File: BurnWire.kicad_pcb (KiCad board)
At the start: 2 copper layers, 44.6 x 45.3 mm, 14 parts, among them J1 B6B-XH-A_LF__SN_, U1 ADP2303ARDZ

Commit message: done layout
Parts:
- moved R3 26.6 mm to (139.1, 75.4), turned to 0 degrees
- moved U1 26.0 mm to (137.8, 88.3), turned to -90 degrees
- moved R1 25.1 mm to (144.7, 93.8)
- moved C3 24.3 mm to (160.8, 79.2)
- moved C4 24.3 mm to (169.8, 79.2)
- moved C5 24.3 mm to (165.8, 88.6)
- moved TP2 23.0 mm to (149.1, 89.5)
- moved R2 20.9 mm to (143.9, 85.0)
- moved J1 19.0 mm to (142.2, 79.7), turned to 180 degrees
- moved CR1 11.8 mm to (157.2, 98.0), turned to 180 degrees
- moved L1 11.4 mm to (153.7, 79.2)
- moved TP1 10.2 mm to (158.6, 106.5)
- moved C2 9.40 mm to (134.6, 98.8)
- moved C1 6.34 mm to (134.4, 106.4)
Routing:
- net /VBatt: track 105.4 -> 34.9 mm
- net /EN: track 47.2 -> 8.22 mm, vias 2 -> 0
- net Net-(U1-SW): track 34.9 -> 68.0 mm, vias 0 -> 2
- net Net-(U1-PGOOD): track 44.7 -> 13.1 mm, vias 2 -> 0
- net GND: track 159.1 -> 165.0 mm
- net /Vout: track 38.6 -> 42.9 mm
- net /VCutN: track 32.6 -> 29.6 mm, vias 0 -> 2
- net Net-(U1-BST): track 21.6 -> 23.9 mm
- net Net-(U1-FB): track 7.55 -> 5.95 mm
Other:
- board size 44.6 x 45.3 mm -> 44.6 x 45.4 mm

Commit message: optimized layout
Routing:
- net GND: track 165.0 -> 161.6 mm
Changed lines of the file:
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@@
-	)
-	(segment
-		(start 158.1685 71.2185)
-		(end 160.35 73.4)
-		(width 0.635)
-		(layer "F.Cu")
-		(net 3)
 	)
 	(segment
@@
 	)
 	(segment
-		(start 143.3815 71.2185)
-		(end 158.1685 71.2185)
-		(width 0.635)
-		(layer "F.Cu")
-		(net 3)
-	)
-	(segment
-		(start 140.75 73.85)
-		(end 143.3815 71.2185)
-		(width 0.635)
-		(layer "F.Cu")
-		(net 3)
-	)
-	(segment
 		(start 136.8 89.27)
 		(end 137.8 88.27)
@@
 	)
 	(segment
-		(start 160.35 73.4)
+		(start 143.851597 73.4)
 		(end 164.9 73.4)
 		(width 0.635)
@@
 	)
 	(segment
-		(start 140.7635 76.8365)
-		(end 140.7635 73.8635)
+		(start 138.4 79.2)
+		(end 138.4 78.851597)
 		(width 0.635)
 		(layer "F.Cu")
@@
 	)
 	(segment
-		(start 140.7635 73.8635)
-		(end 140.75 73.85)
-		(width 0.635)
-		(layer "F.Cu")
-		(net 3)
-	)
-	(segment
 		(start 164.583431 108.7535)
 		(end 166.5 106.836931)
@@
 	)
 	(segment
+		(start 138.4 78.851597)
+		(end 143.851597 73.4)
+		(width 0.635)
+		(layer "F.Cu")
+		(net 3)
+	)
+	(segment
 		(start 149.55 101.047692)
 		(end 149.55 98.7925)
@@
 		(width 0.635)
 		(layer "F.Cu")
-		(net 3)
-	)
-	(segment
-		(start 138.4 79.2)
-		(end 140.7635 76.8365)
-		(width 0.635)
-		(layer "F.Cu")

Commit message: generated gerber
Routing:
- net GND: track 161.6 -> 167.7 mm
- net /Vout: track 42.9 -> 47.6 mm
- net /VBatt: track 34.9 -> 35.6 mm

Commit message: redid layout
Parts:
- moved L1 32.8 mm to (141.5, 109.7)
- moved C1 28.6 mm to (163.1, 105.9), turned to 180 degrees
- moved C2 28.3 mm to (162.8, 99.0), turned to 180 degrees
- moved U1 18.3 mm to (155.6, 92.7), turned to 180 degrees
- moved CR1 17.4 mm to (169.4, 110.4)
- moved TP2 16.9 mm to (140.6, 104.2)
- moved R2 13.1 mm to (135.2, 94.7)
- moved R3 10.5 mm to (137.9, 85.8)
- moved TP1 7.08 mm to (153.1, 111.0)
- moved C4 4.32 mm to (168.6, 83.3)
- moved C5 4.23 mm to (168.6, 91.8)
- moved R1 3.80 mm to (143.9, 97.5), turned to -90 degrees
- moved C3 3.76 mm to (158.8, 82.4)
- moved J1 1.68 mm to (141.7, 81.3)
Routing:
- net /EN: track 8.22 -> 100.3 mm
- net GND: track 167.7 -> 87.8 mm
- net Net-(U1-SW): track 68.0 -> 27.4 mm, vias 2 -> 0
- net /VBatt: track 35.6 -> 14.4 mm
- net Net-(U1-FB): track 5.95 -> 23.8 mm
- net /VCutN: track 29.4 -> 44.5 mm, vias 2 -> 0
- net /Vout: track 47.6 -> 33.8 mm
- net Net-(U1-BST): track 23.9 -> 13.4 mm
- net Net-(U1-PGOOD): track 13.1 -> 21.7 mm

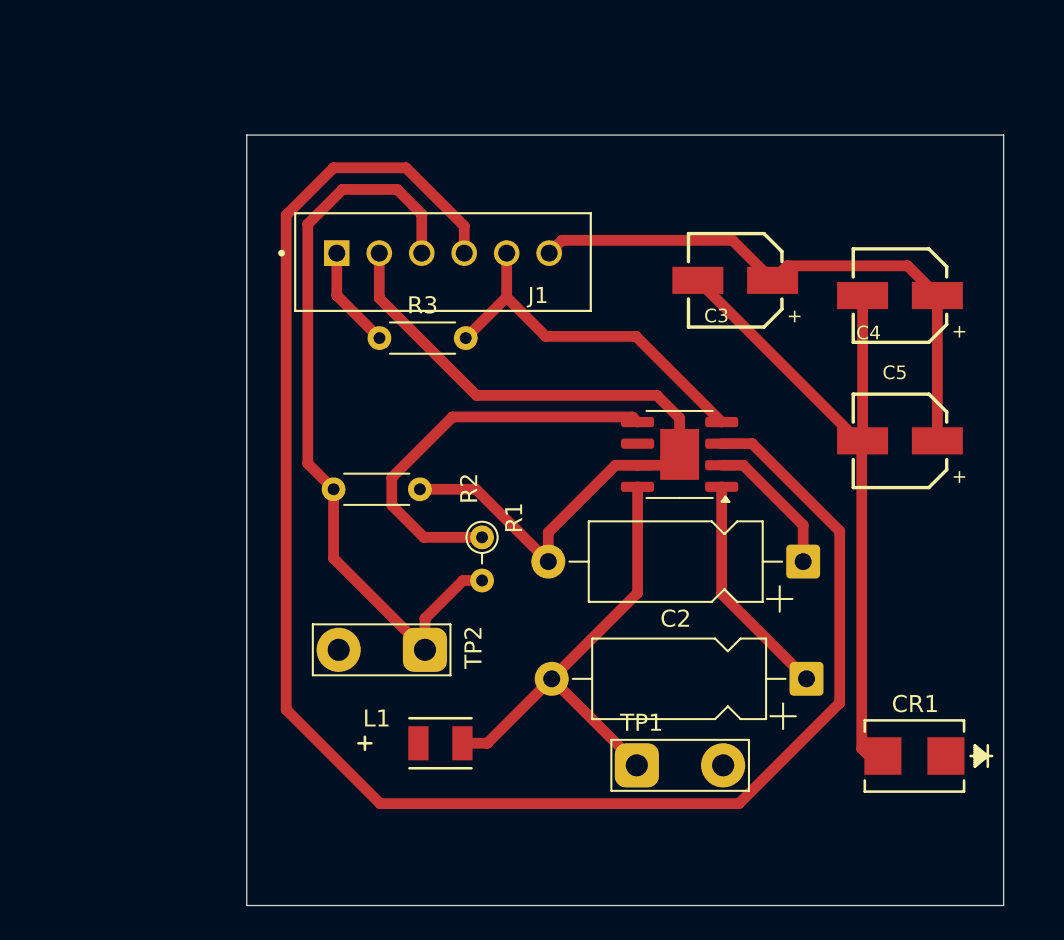
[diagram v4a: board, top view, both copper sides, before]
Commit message: finished one-layer layout
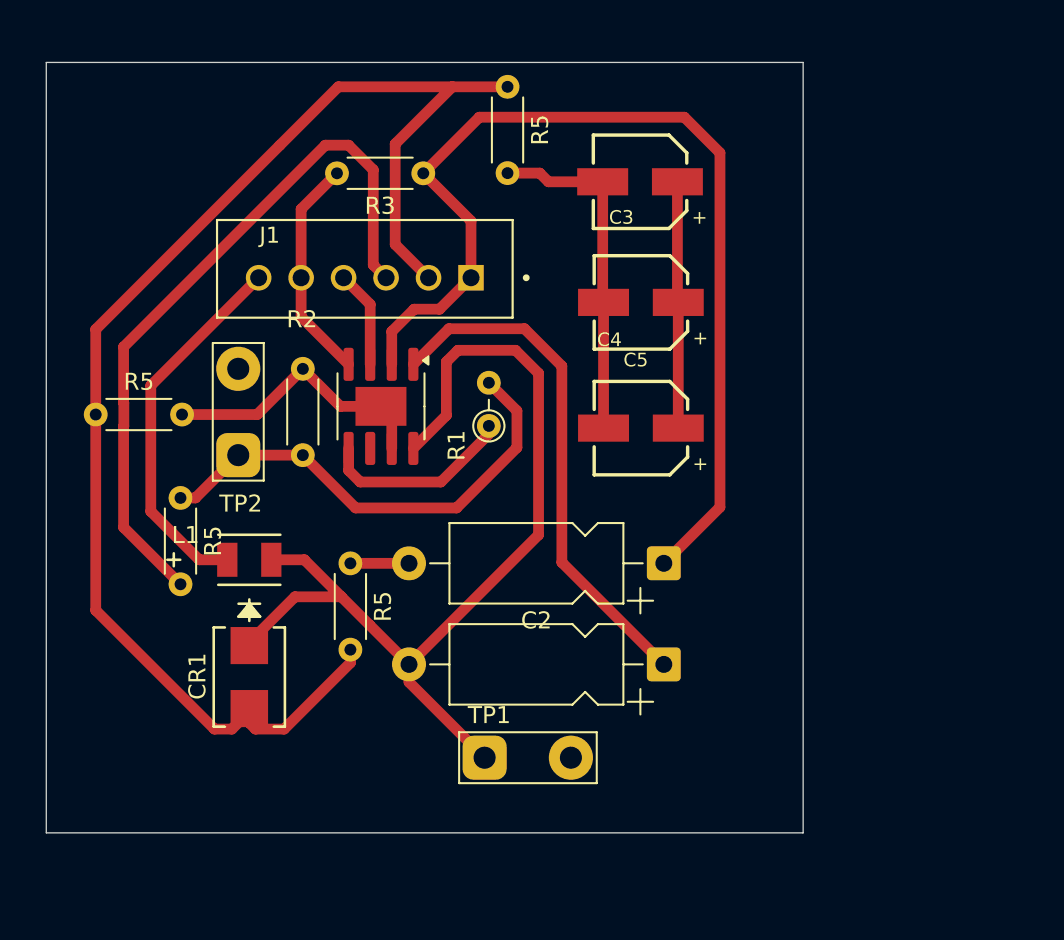
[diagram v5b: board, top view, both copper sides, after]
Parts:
- added R5: 0K, Resistor_THT:R_Axial_DIN0204_L3.6mm_D1.6mm_P5.08mm_Horizontal, F.Cu at (126.2, 95.2)
- added R5: 0K, Resistor_THT:R_Axial_DIN0204_L3.6mm_D1.6mm_P5.08mm_Horizontal, F.Cu at (136.2, 99.1)
- added R5: 0K, Resistor_THT:R_Axial_DIN0204_L3.6mm_D1.6mm_P5.08mm_Horizontal, F.Cu at (121.2, 90.3)
- added R5: 0K, Resistor_THT:R_Axial_DIN0204_L3.6mm_D1.6mm_P5.08mm_Horizontal, F.Cu at (145.4, 71.0)
- moved CR1 39.4 mm to (130.2, 105.8), turned to -90 degrees
- moved U1 17.8 mm to (138.0, 89.8), turned to -90 degrees
- moved TP2 15.9 mm to (129.6, 92.7), turned to 90 degrees
- moved L1 15.6 mm to (130.2, 98.8)
- moved C5 15.3 mm to (153.3, 91.1)
- moved C4 15.3 mm to (153.3, 83.7)
- moved R3 10.0 mm to (140.5, 76.1), turned to 180 degrees
- moved TP1 8.97 mm to (144.1, 110.5)
- moved C1 8.44 mm to (154.7, 105.0)
- moved C2 8.20 mm to (154.7, 99.1)
- moved C3 8.06 mm to (153.2, 76.6)
- moved R1 6.57 mm to (144.3, 91.0), turned to 90 degrees
- moved J1 4.62 mm to (137.1, 81.7), turned to 0 degrees
- moved R2 2.70 mm to (133.4, 92.7), turned to 90 degrees
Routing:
- net /EN: track 100.3 -> 5.74 mm
- net /VBatt: track 14.4 -> 60.4 mm
- net GND: track 87.8 -> 122.3 mm
- net Net-(U1-SW): track 27.4 -> 57.2 mm
- net /VCutN: track 44.5 -> 70.4 mm
- net Net-(U1-BST): track 13.4 -> 30.6 mm
- net Net-(U1-FB): track 23.8 -> 11.5 mm
- net Net-(U1-PGOOD): track 21.7 -> 13.3 mm
- net /Vout: track 33.8 -> 36.6 mm
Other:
- board size 44.6 x 45.4 mm -> 44.5 x 45.3 mm

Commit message: Edit via size, connect Vout
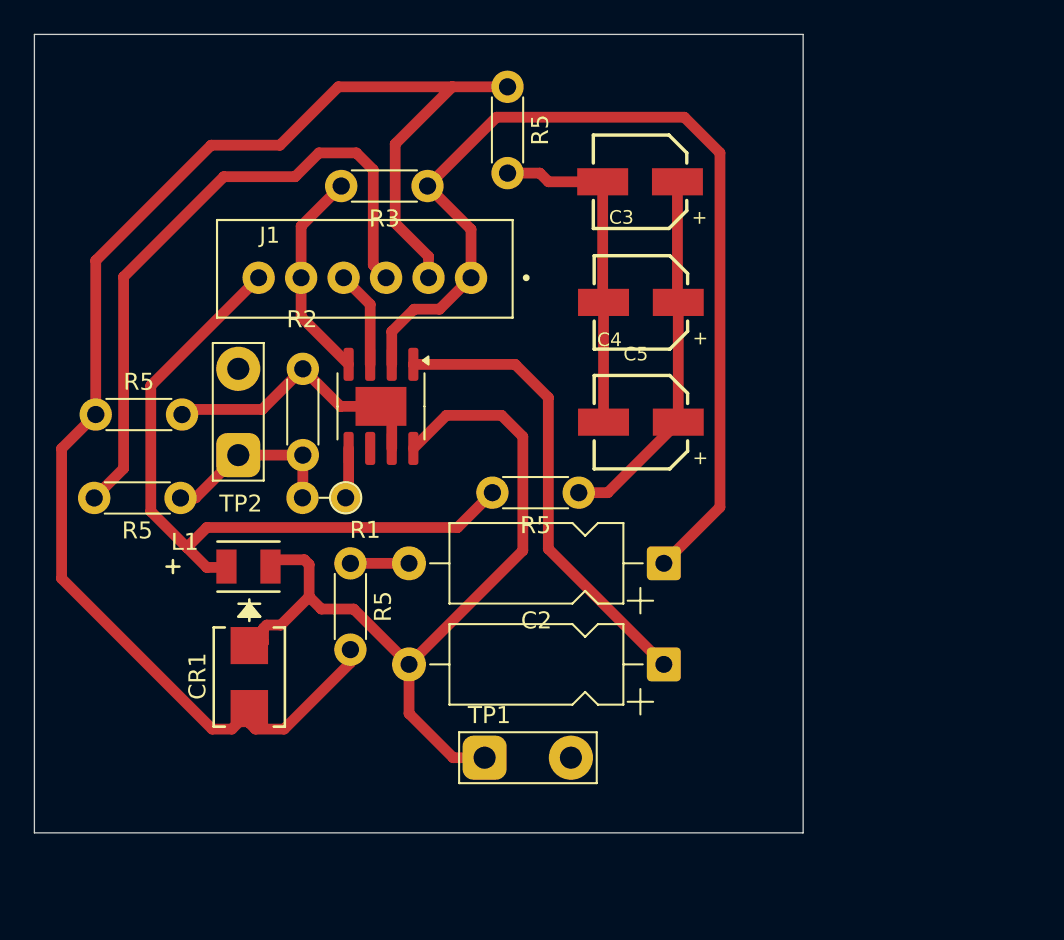
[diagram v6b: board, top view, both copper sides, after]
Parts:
- added R5: 0K, Resistor_THT:R_Axial_DIN0204_L3.6mm_D1.6mm_P5.08mm_Horizontal, F.Cu at (149.6, 94.9)
- moved R1 9.43 mm to (135.9, 95.2), turned to 180 degrees
- moved R3 0.79 mm to (140.7, 76.8)
- moved L1 0.40 mm to (130.2, 99.2)
- moved C5 0.35 mm to (153.3, 90.8)
- turned R5 to 180 degrees
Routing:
- net /Vout: track 36.6 -> 63.6 mm
- net /VCutN: track 70.4 -> 49.9 mm
- net Net-(U1-FB): track 11.5 -> 3.63 mm
- net Net-(U1-SW): track 57.2 -> 49.3 mm
- net GND: track 122.3 -> 126.4 mm
- net Net-(U1-BST): track 30.6 -> 27.3 mm
- net /VBatt: track 60.4 -> 59.7 mm
- net Net-(U1-PGOOD): track 13.3 -> 12.6 mm
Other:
- board size 44.5 x 45.3 mm -> 45.2 x 47 mm

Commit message: Changes for manufacturing
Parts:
- moved CR1 2.15 mm to (130.3, 107.9)
- moved L1 1.57 mm to (131.0, 100.6)
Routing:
- net Net-(U1-SW): track 49.3 -> 47.4 mm
- net /Vout: track 63.6 -> 65.0 mm
- net GND: track 126.4 -> 125.6 mm
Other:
- board size 45.2 x 47 mm -> 43.8 x 45.8 mm

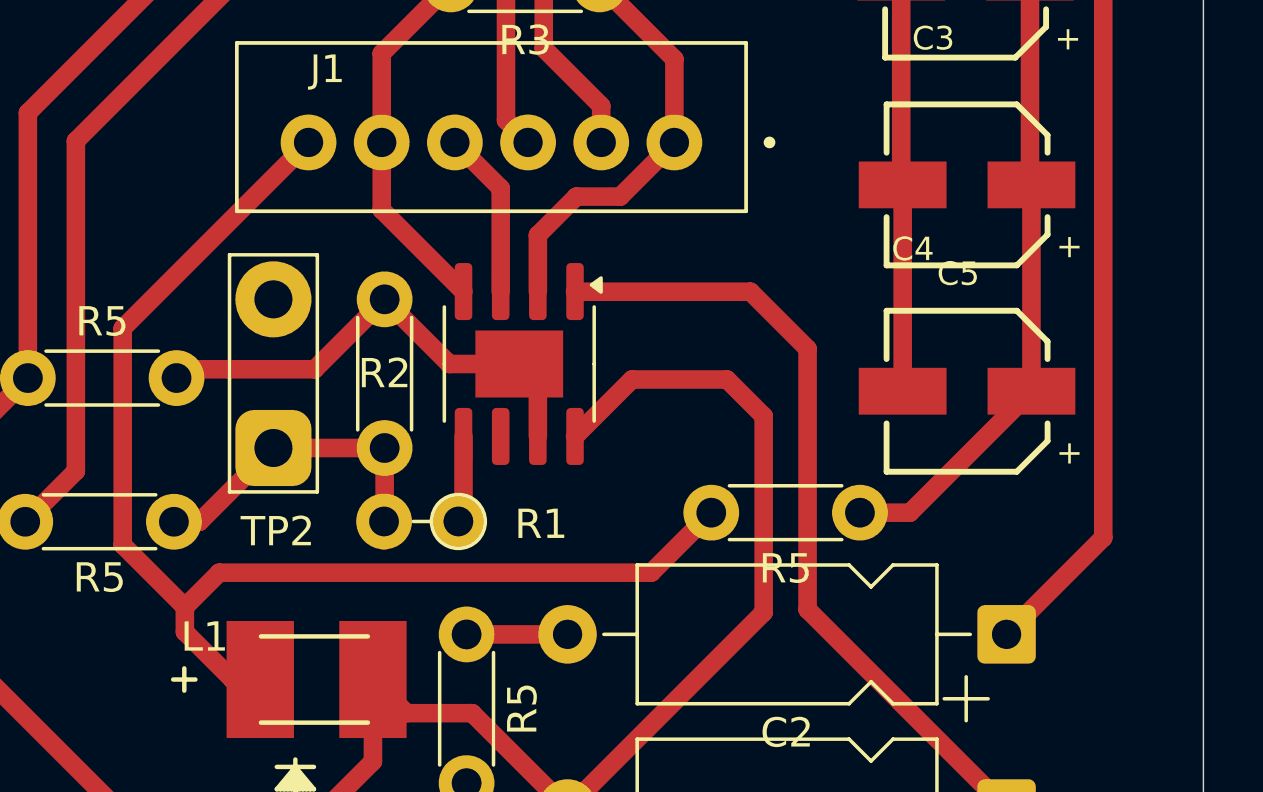
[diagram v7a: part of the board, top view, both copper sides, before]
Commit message: Polished schema w/ labels, test points; updated layout for new Vout->FB VDivider
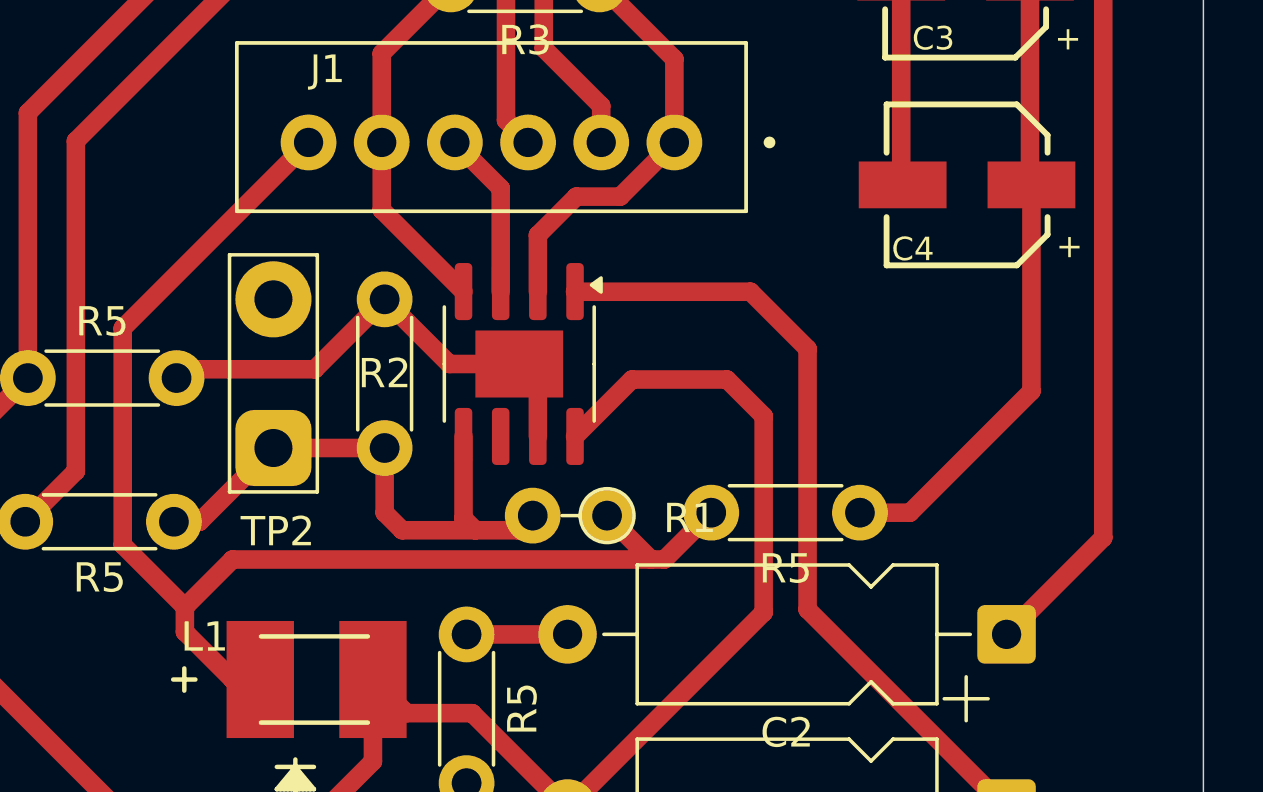
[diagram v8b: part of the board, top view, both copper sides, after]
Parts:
- removed C5: WCAP-ASLI_5X5.5, WCAP-ASLI:WCAP-ASLI_5X5.5_DXL_
- R2: value 0.5 -> 10K
- moved R1 5.08 mm to (141.0, 95.0)
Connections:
- net Net-(U1-BST) renamed BST
- net Net-(U1-PGOOD) renamed PGOOD
- net Net-(U1-SW) renamed SW
- R1 pad 1: Net-(U1-FB) -> /Vout
- U1 pad 5: Net-(U1-FB) -> /VCutN
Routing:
- net /VCutN: track 49.9 -> 57.9 mm
- net GND: track 125.6 -> 118.2 mm
- net Net-(U1-FB): track 3.63 -> 0.00 mm
- net /Vout: track 65.0 -> 67.2 mm
